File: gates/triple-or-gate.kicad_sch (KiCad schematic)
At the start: 0 parts

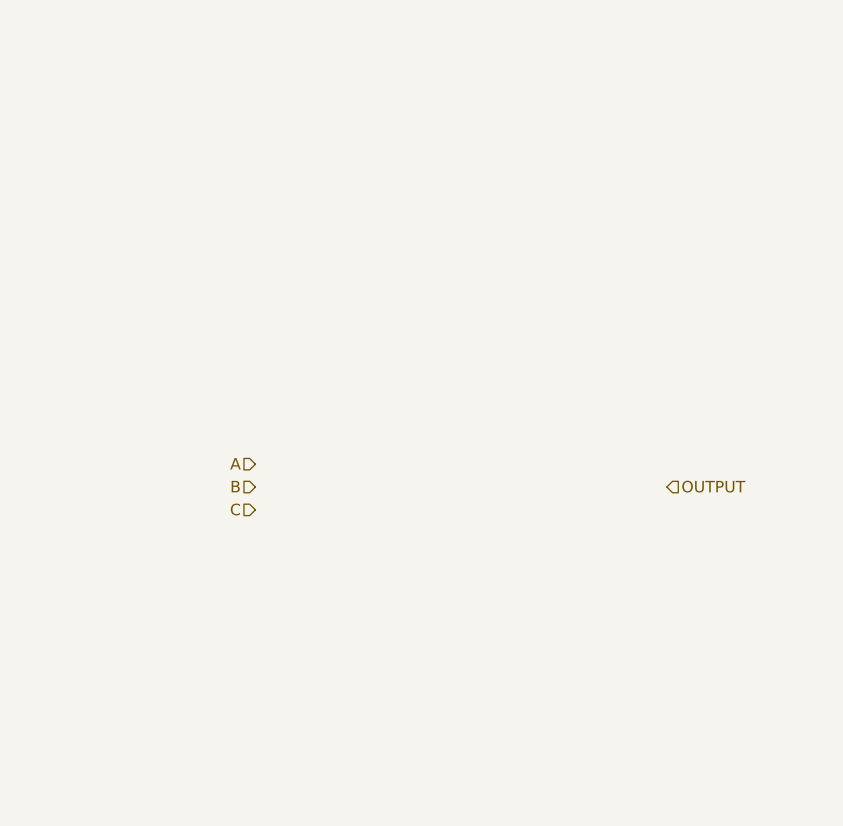
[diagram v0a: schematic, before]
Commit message: Fix ADD command logic for control-unit
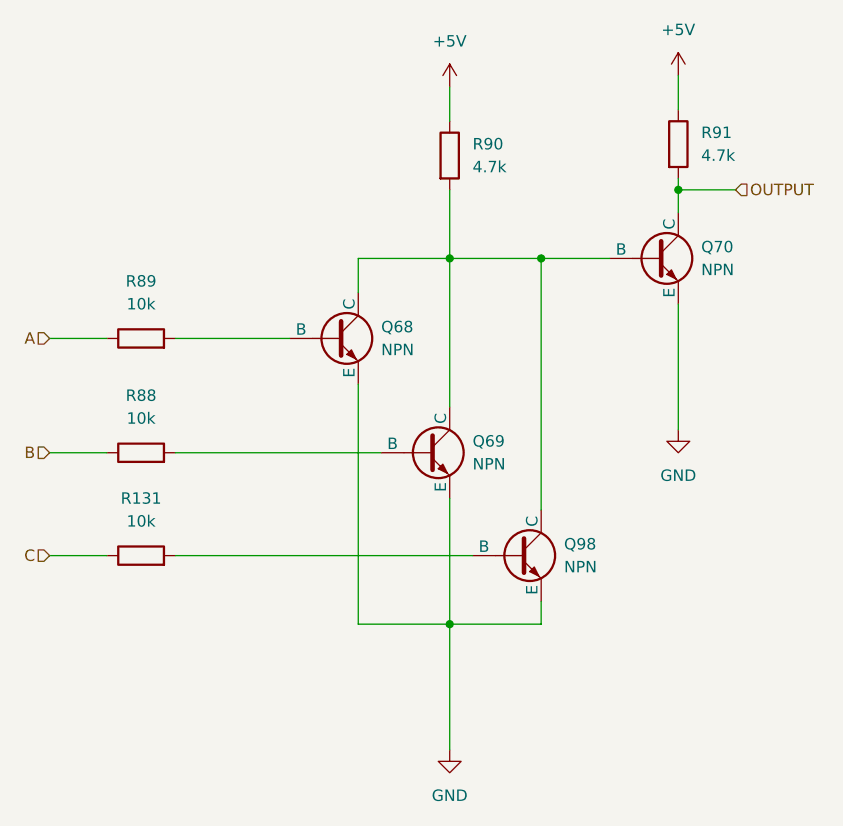
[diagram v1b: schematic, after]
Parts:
- added Q68, Q69, Q70, Q98: NPN, SOT-23-3_L2.9-W1.6-P1.90-LS2.8-BR:SOT-23-3_L2.9-W1.6-P1.90-LS2.8-BR, symbol Simulation_SPICE:NPN
- added R131, R88, R89: 10k, R0603:R0603, symbol Device:R
- added R90, R91: 4.7k, R0603:R0603, symbol Device:R
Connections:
- net A: now also R89.1
- net B: now also R88.1
- net C: now also R131.1
- net OUTPUT: now also Q70.1 (C), R91.2
- new net: Q68.1 (C), Q69.1 (C), Q70.2 (B), Q98.1 (C), R90.2
- new net: Q68.2 (B), R89.2
- new net: Q98.2 (B), R131.2
- new net: Q69.2 (B), R88.2
- new net +5V: R90.1, R91.1
- new net GND: Q68.3 (E), Q69.3 (E), Q70.3 (E), Q98.3 (E)
